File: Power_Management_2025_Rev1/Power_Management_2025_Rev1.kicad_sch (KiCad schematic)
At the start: 10 parts, among them U1 Teensy4.1_DEV-16771, U2 OKI-78SR-3.3_1.5-W36-C, U3 ACS756xCB-050B-PFF, U4 OKI-78SR-5_1.5-W36-C

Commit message: worked on PDR schmadic
Worked on current sensors and buzzer and put together RJ-45
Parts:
- removed C4: C, symbol Device:C
- removed U4: OKI-78SR-5_1.5-W36-C, Converter_DCDC:Converter_DCDC_Murata_OKI-78SR_Vertical, symbol Converter_DCDC:OKI-78SR-5_1.5-W36-C
- added B1: Buzzer, symbol MRDT_Devices:Buzzer
- added C4, C6, C7: 1000uF, symbol Device:C_Polarized_Small_US
- added C5: 1000uf, symbol Device:C_Polarized_Small_US
- added D1, D2: ~, symbol Device:D
- added D3: RED, symbol Device:LED
- added J1: RJ45_LED_Shielded, symbol Connector:RJ45_LED_Shielded
- added Q1: BSS138, Package_TO_SOT_SMD:SOT-23, symbol Transistor_FET:BSS138
- added R1: 100, symbol Device:R
- added R2: 4.7k, symbol Device:R
- added V1, V2, V3, V4: Via, symbol MRDT_Drill_Holes:Via
- C3: value C -> 0.1uF
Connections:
- net +5V is gone; now on net +3.3V: U3.1 (VCC)
- net CELL_SENSE_- is gone; now on net +24V: U3.5 (IP-)
- net +24V: no longer C3.1
- net +3.3V: now also B1.2 (V-), R1.1
- net GND: now also C4.2, C5.2, C6.2, C7.2, D1.2 (A), D2.2 (A), J1.8, J1.9, J1.SH, Q1.2 (S), R2.2
- net LED: now reaches U1.LED
- net LED: now also J1.10
- net RX+: now reaches U1.R+
- net RX+: now also J1.4
- net RX-: now reaches U1.R-
- net RX-: now also J1.6
- net TX+: now reaches U1.T+
- net TX+: now also J1.1
- net TX-: now reaches U1.T-
- net TX-: now also J1.3
- net CELL_SENSE_+ renamed PV
- net PV: now also C4.1, C5.1, C6.1, C7.1, D1.1 (K), D2.1 (K)
- new net: B1.1 (V+), D3.1 (K), Q1.3 (D)
- new net: D3.2 (A), R1.2
- new net: C3.1, J1.2
- new net Buzzer: Q1.1 (G), R2.1
- no-connect marks 0 -> 3
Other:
- note added: "VIA's for mounting"
- moved on the sheet: C1, C2, Conn1A, Conn1D, Conn2, U1, U2, U3

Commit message: Added components
Added cell sensing opamps, LC and motor gate drivers, external current sense.
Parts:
- added C8, C9: 10uF, symbol Device:C
- added Conn3: Molex_SL_03, symbol MRDT_Connectors:Molex_SL_03
- added Q2, Q3: IPB180N10S4-02, Package_TO_SOT_SMD:TO-263-6, symbol Transistor_FET:IPB180N10S4-02
- added R10, R11, R14, R15, R18, R19, R22, R23, R26, R4, R6, R7: 11k, symbol Device:R
- added R12, R13, R16, R17, R20, R21, R24, R25, R3, R5, R8, R9: 14k, symbol Device:R
- added R27, R28: 5.1k, symbol Device:R
- added U10, U11: LT1910, symbol MRDT_ICs:LT1910
- added U4, U5, U6, U7, U8, U9: ${SIM.PARAMS}, symbol Simulation_SPICE:OPAMP
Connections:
- net +24V: no longer Conn1.4 (PV+)
- net +3.3V: now also Conn3.1
- net Buzzer: now also U1.22 (A8)
- net GND: now also C8.2, C9.2, Conn3.3, R11.2, R15.2, R19.2, R23.2, R3.2, R6.2, R7.2, U10.1 (GND), U10.2 (TIMER), U11.1 (GND), U11.2 (TIMER), U4.4 (V-), U5.4 (V-), U6.4 (V-), U7.4 (V-), U8.4 (V-), U9.4 (V-)
- net PV: now also C8.1, C9.1, Q2.4 (D), Q3.4 (D), U10.8 (V+), U11.8 (V+), U4.3 (V+), U5.3 (V+), U6.3 (V+), U7.3 (V+), U8.3 (V+), U9.3 (V+)
- net Cell_Sense1: now reaches U1.15 (A1)
- net Cell_Sense1: now also R4.1, U7.5
- net Cell_Sense2: now reaches U1.16 (A2)
- net Cell_Sense2: now also R10.1, U4.5
- net Cell_Sense3: now reaches U1.17 (A3)
- net Cell_Sense3: now also R14.1, U5.5
- net Cell_Sense4: now reaches U1.18 (A4)
- net Cell_Sense4: now also R18.1, U6.5
- net Cell_Sense5: now reaches U1.19 (A5)
- net Cell_Sense5: now also R22.1, U8.5
- net Cell_Sense6: now reaches U1.20 (A6)
- net Cell_Sense6: now also R26.1, U9.5
- new net: R11.1, R12.1, U5.1 (+)
- new net: R10.2, R9.1, U4.2 (-)
- new net: R5.1, R6.1, U7.1 (+)
- new net: R3.1, R4.2, U7.2 (-)
- new net: Q2.1 (G), U10.5 (GATE)
- new net: R25.1, R26.2, U9.2 (-)
- new net: R7.1, R8.1, U4.1 (+)
- new net: R17.1, R18.2, U6.2 (-)
- new net: R19.1, R20.1, U8.1 (+)
- new net: R21.1, R22.2, U8.2 (-)
- new net: R23.1, R24.1, U9.1 (+)
- new net: R15.1, R16.1, U6.1 (+)
- new net: R13.1, R14.2, U5.2 (-)
- new net: R28.2, U11.3 (FAULT)
- new net: R27.2, U10.3 (FAULT)
- new net: Q3.1 (G), U11.5 (GATE)
- new net +5V: R27.1, R28.1
- new net +BATT: Conn1.4 (PV+)
- new net Cell1: R5.2, R9.2
- new net Cell2: R13.2, R8.2
- new net Cell3: R12.2, R17.2
- new net Cell4: R16.2, R21.2
- new net Cell5: R20.2, R25.2
- new net Cell6: R24.2
- new net Current_Sense: Conn3.2
- new net LC_en: U10.4 (IN)
- new net Low_Current_PWR: Q2.2 (S), Q2.3 (S), Q2.5 (S), Q2.6 (S), Q2.7 (S)
- new net M_Power: Q3.2 (S), Q3.3 (S), Q3.5 (S), Q3.6 (S), Q3.7 (S)
- new net Motor_en: U11.4 (IN)

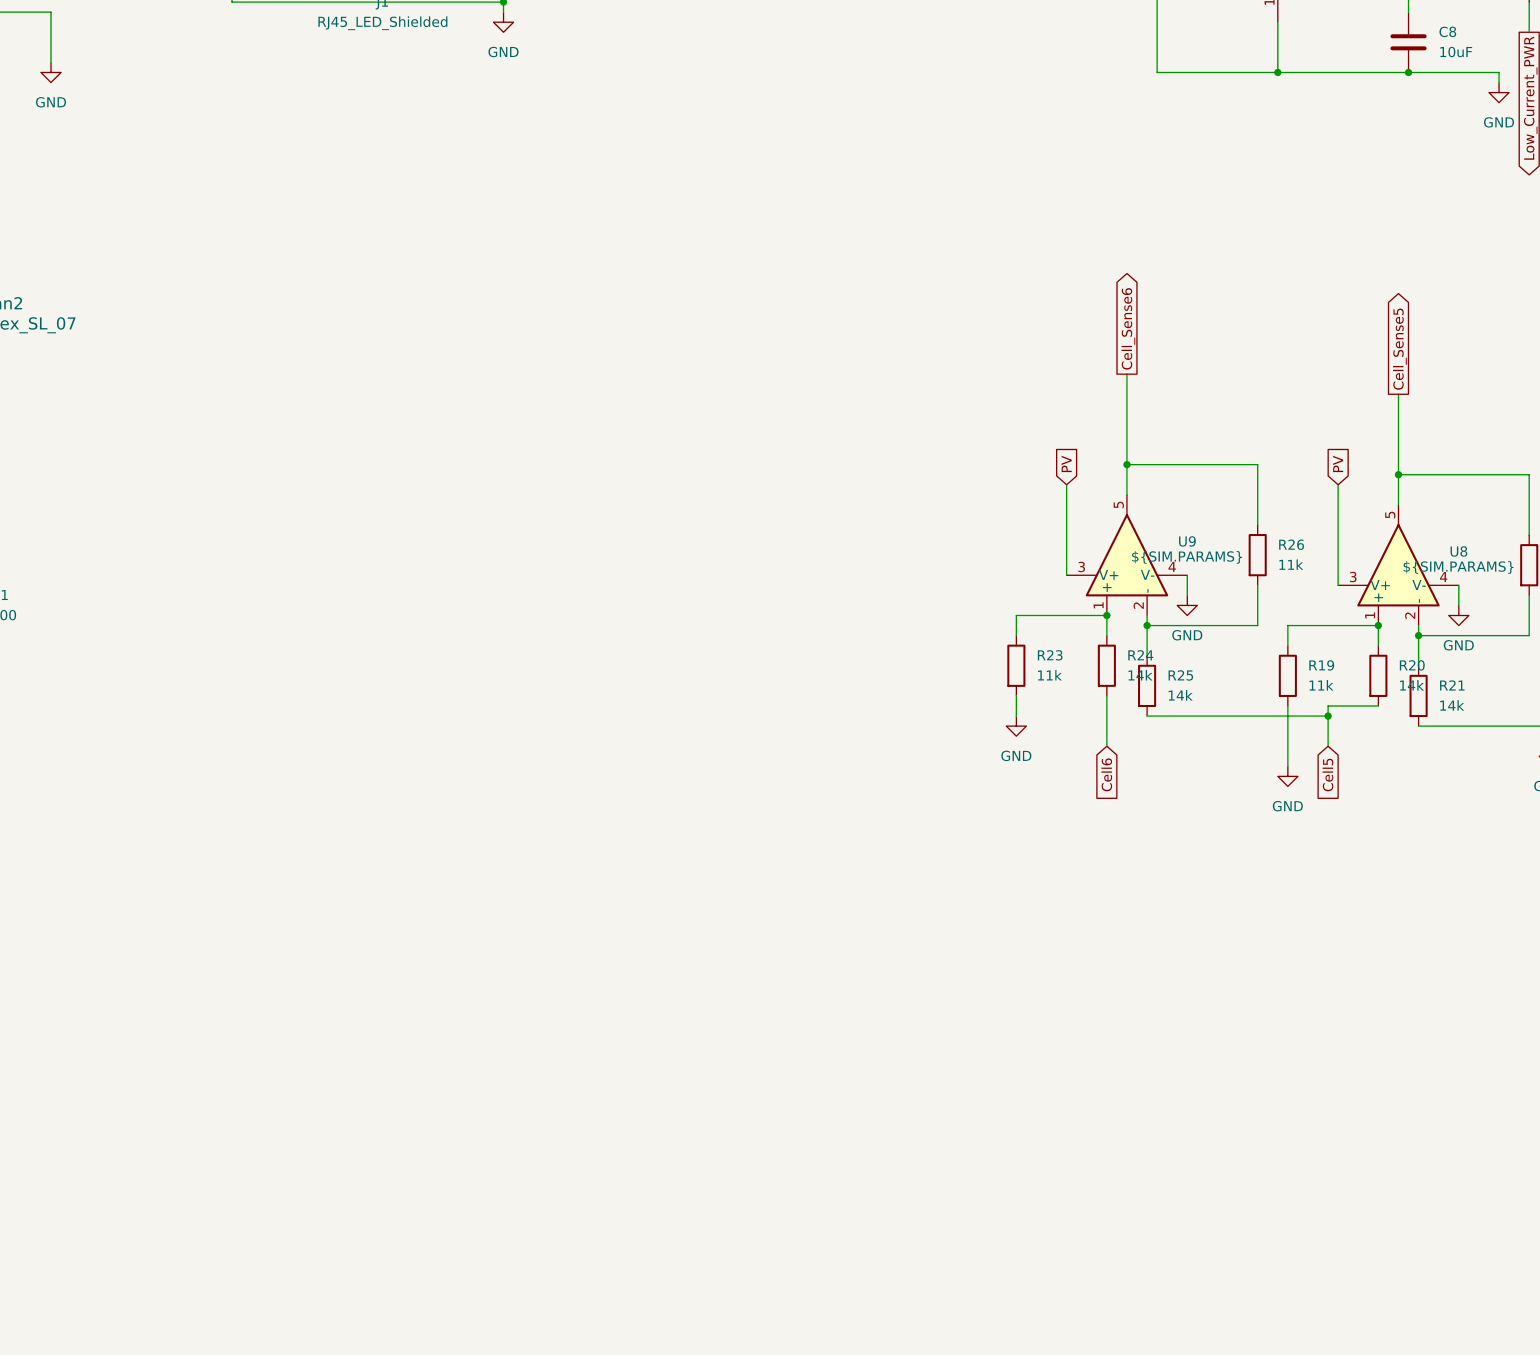
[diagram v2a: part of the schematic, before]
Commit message: Transfered Fun2 to PMS 2025
It worked if you make a new project you can copy and paste into other projects
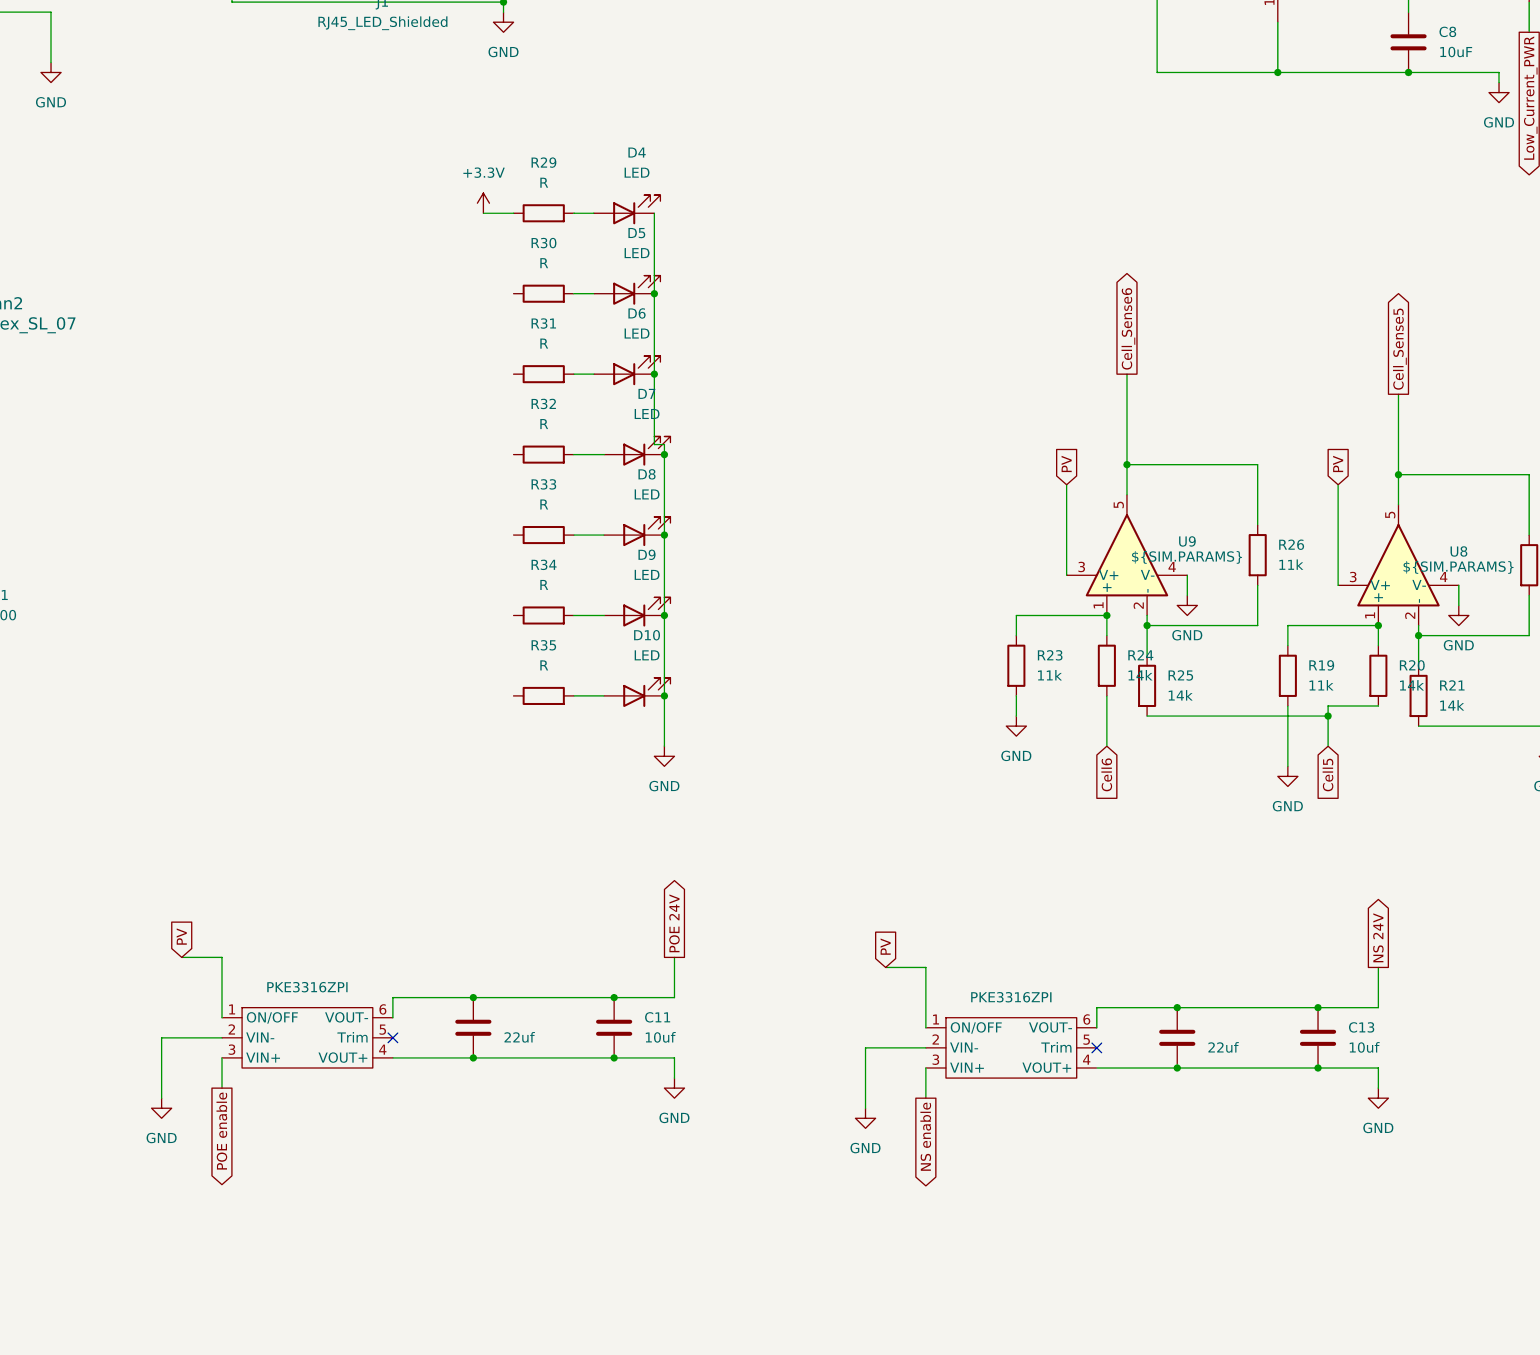
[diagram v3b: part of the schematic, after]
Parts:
- added C10, C12: 22uf, symbol Device:C
- added C11, C13: 10uf, symbol Device:C
- added D10, D4, D5, D6, D7, D8, D9: LED, symbol Device:LED
- added R29, R30, R31, R32, R33, R34, R35: R, symbol Device:R
- added U12, U13: PKE3316ZPI, symbol MRDT_Devices:PKE3316ZPI
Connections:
- net +3.3V: now also R29.1
- net GND: now also C10.2, C11.2, C12.2, C13.2, D10.1 (K), D4.1 (K), D5.1 (K), D6.1 (K), D7.1 (K), D8.1 (K), D9.1 (K), U12.2 (VIN-), U12.4 (VOUT+), U13.2 (VIN-), U13.4 (VOUT+)
- net PV: now also U12.1 (ON/OFF), U13.1 (ON/OFF)
- new net: D6.2 (A), R31.2
- new net: D4.2 (A), R29.2
- new net: D9.2 (A), R34.2
- new net: D5.2 (A), R30.2
- new net: D10.2 (A), R35.2
- new net: D8.2 (A), R33.2
- new net: D7.2 (A), R32.2
- new net NS 24V: C12.1, C13.1, U13.6 (VOUT-)
- new net NS enable: U13.3 (VIN+)
- new net POE 24V: C10.1, C11.1, U12.6 (VOUT-)
- new net POE enable: U12.3 (VIN+)
- no-connect marks 3 -> 5

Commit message: Pausing work for a bit
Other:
- note added: "TEENSY"
- moved on the sheet: B1, C1, C11, C13, C2, C3, C4, C5, C6, C7, C8, C9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

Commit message: More formating done
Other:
- note added: "Current Sensing"
- note added: "NS 24V"
- note added: "POE 24V"
- moved on the sheet: B1, C11, C13, C4, C5, C6, C7, C8, C9, Conn2, Conn3, D1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

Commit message: more format
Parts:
- added Conn10, Conn11, Conn12, Conn13, Conn14, Conn15, Conn16, Conn17, Conn18, Conn4, Conn5, Conn6, Conn7, Conn8, Conn9: AndersonPP, MRDT_Connectors:Square_Anderson_2_H_Stacked, symbol MRDT_Connectors:AndersonPP
- R29, R30, R31, R32, R33, R34, R35: value R -> 2k
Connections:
- net GND: now also Conn10.1 (GND), Conn11.1 (GND), Conn12.1 (GND), Conn13.1 (GND), Conn14.1 (GND), Conn15.1 (GND), Conn16.1 (GND), Conn17.1 (GND), Conn18.1 (GND), Conn4.1 (GND), Conn5.1 (GND), Conn6.1 (GND), Conn7.1 (GND), Conn8.1 (GND), Conn9.1 (GND)
- net PV: now also R35.1
- net POE_24V: now reaches R31.1
- net POE_24V: now also Conn13.4 (PV+)
- net NS_24V: now reaches R30.1
- net NS_24V: now also Conn12.4 (PV+)
- net LowCurrent_PWR: now reaches R34.1
- net LowCurrent_PWR: now also Conn14.4 (PV+), Conn15.4 (PV+), Conn16.4 (PV+), Conn17.4 (PV+), Conn18.4 (PV+)
- net Motor_PWR: now reaches R32.1
- net Motor_PWR: now also Conn10.4 (PV+), Conn4.4 (PV+), Conn5.4 (PV+), Conn6.4 (PV+), Conn7.4 (PV+), Conn8.4 (PV+), Conn9.4 (PV+)
- net Aux_PWR: now reaches R33.1
- net Aux_PWR: now also Conn11.4 (PV+)
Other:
- note added: "Andersons"
- note added: "Battery Cells"
- note added: "Buzzer Circuit"
- note added: "OKI 3.3V"
- note added: "Status LEDs"
- moved on the sheet: B1, C1, C2, C4, C5, C6, C7, C8, C9, Conn2, Conn3, D1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

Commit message: Added few components and cleaned up schematic
Added few more andersons and cleaned up schematic
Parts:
- added unit 5 of Conn1
- added Conn19, Conn20, Conn21, Conn22: AndersonPP, symbol MRDT_Connectors:AndersonPP
- added unit 5 of Conn4
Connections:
- net +24V: no longer U3.5 (IP-)
- net +BATT: now also U3.5 (IP-)
- net GND: now also Conn19.1 (GND), Conn20.1 (GND), Conn21.1 (GND), Conn22.1 (GND)
- net PV: now also Conn1.1, Conn19.4 (PV+), Conn20.4 (PV+), Conn4.1
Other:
- note added: "Bank"
- note added: "Connectors"
- note added: "Low Current Gate Driver"
- note added: "Motor Gate Driver"
- moved on the sheet: B1, C1, C2, Conn10A, Conn10D, Conn11A, Conn11D, Conn12A, Conn12D, Conn13A, Conn13D, Conn14A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

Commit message: Corrected POE and NS converter
and added signal labels
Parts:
- added Conn23: Molex_SL_03, symbol MRDT_Connectors:Molex_SL_03
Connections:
- net NS enable is gone; now on net PV: U13.3 (VIN+)
- net POE enable is gone; now on net PV: U12.3 (VIN+)
- net +3.3V: now also Conn23.1
- net GND: now also C10.1, C11.1, C12.1, C13.1, U12.6 (VOUT-), U13.6 (VOUT-), Conn23.3; no longer C10.2, C11.2, C12.2, C13.2, U12.4 (VOUT+), U13.4 (VOUT+)
- net Motor_en: now also U1.32 (OUT1B)
- net NS 24V: now also C12.2, C13.2, U13.4 (VOUT+); no longer C12.1, C13.1, U13.6 (VOUT-)
- net POE 24V: now also C10.2, C11.2, U12.4 (VOUT+); no longer C10.1, C11.1, U12.6 (VOUT-)
- net PV: no longer U12.1 (ON/OFF), U13.1 (ON/OFF)
- net POE_Enable: now reaches U1.0 (RX1)
- net POE_Enable: now also U12.1 (ON/OFF)
- net NS_Enable: now reaches U1.1 (TX1)
- net NS_Enable: now also U13.1 (ON/OFF)
- new net Temp_sense: Conn23.2
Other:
- moved on the sheet: C4, C5, C6, C7, Conn3, D1, D2
